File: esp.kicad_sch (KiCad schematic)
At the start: 13 parts, among them U3 ESP32-S3, U8 W25Q16JVUUIQ, Y1 40MHz 10pF

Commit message: finished Layout, started PCB design agound ESP32
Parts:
- added C24, C25: C, Capacitor_SMD:C_0402_1005Metric, symbol Device:C
- added L4: L, Inductor_SMD:L_0402_1005Metric, symbol Device:L
- added U9: RFANT3216120A5T, EasyEda:FILTER-SMD_1206-2P-L3.2-W1.6-L, symbol EasyEda:RFANT3216120A5T
- U8: footprint EasyEDA:USON-8_L4.0-W3.0-P0.80-BL_AT25SL321 -> EasyEda:USON-8_L4.0-W3.0-P0.80-BL_AT25SL321
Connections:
- net +3V3: now also U3.4 (CHIP_PU)
- net GND: now also C24.2, C25.2
- net at U3.1 (LNA_IN): now also C24.1, L4.1
- new net: C25.1, L4.2, U9.1
- no-connect marks 8 -> 9

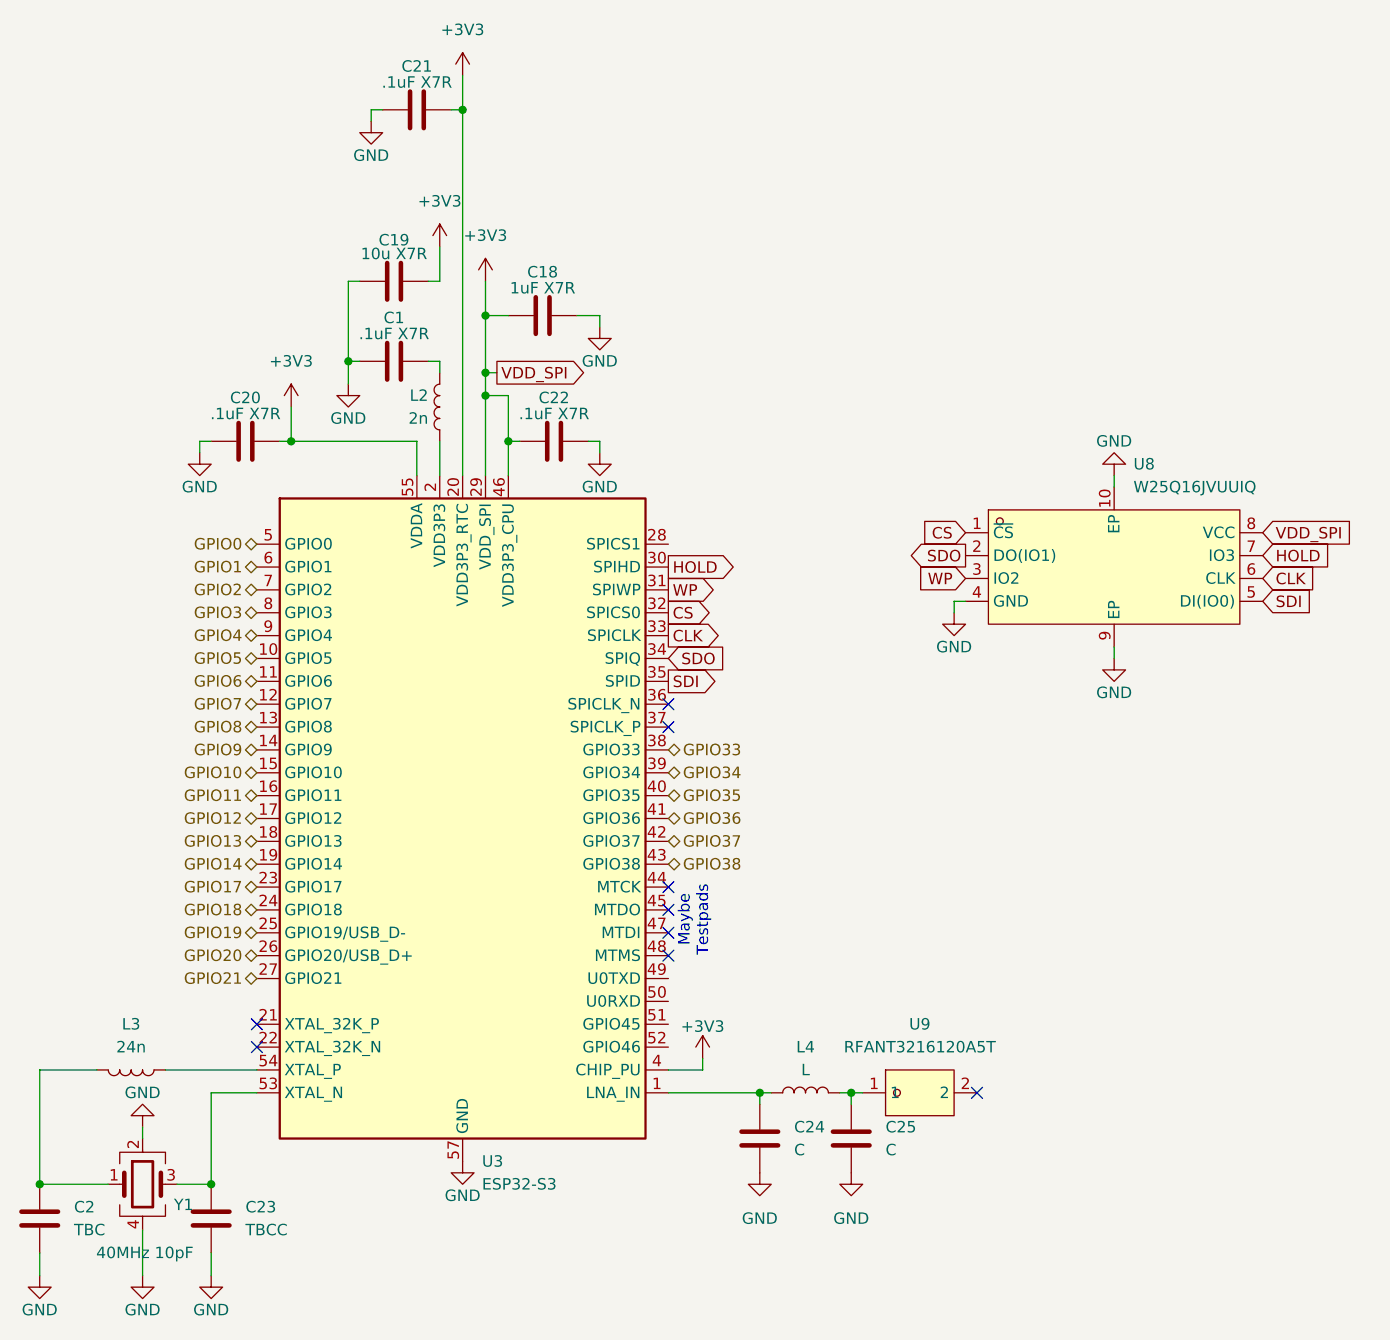
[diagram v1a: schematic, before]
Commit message: pcb parts placed not connected
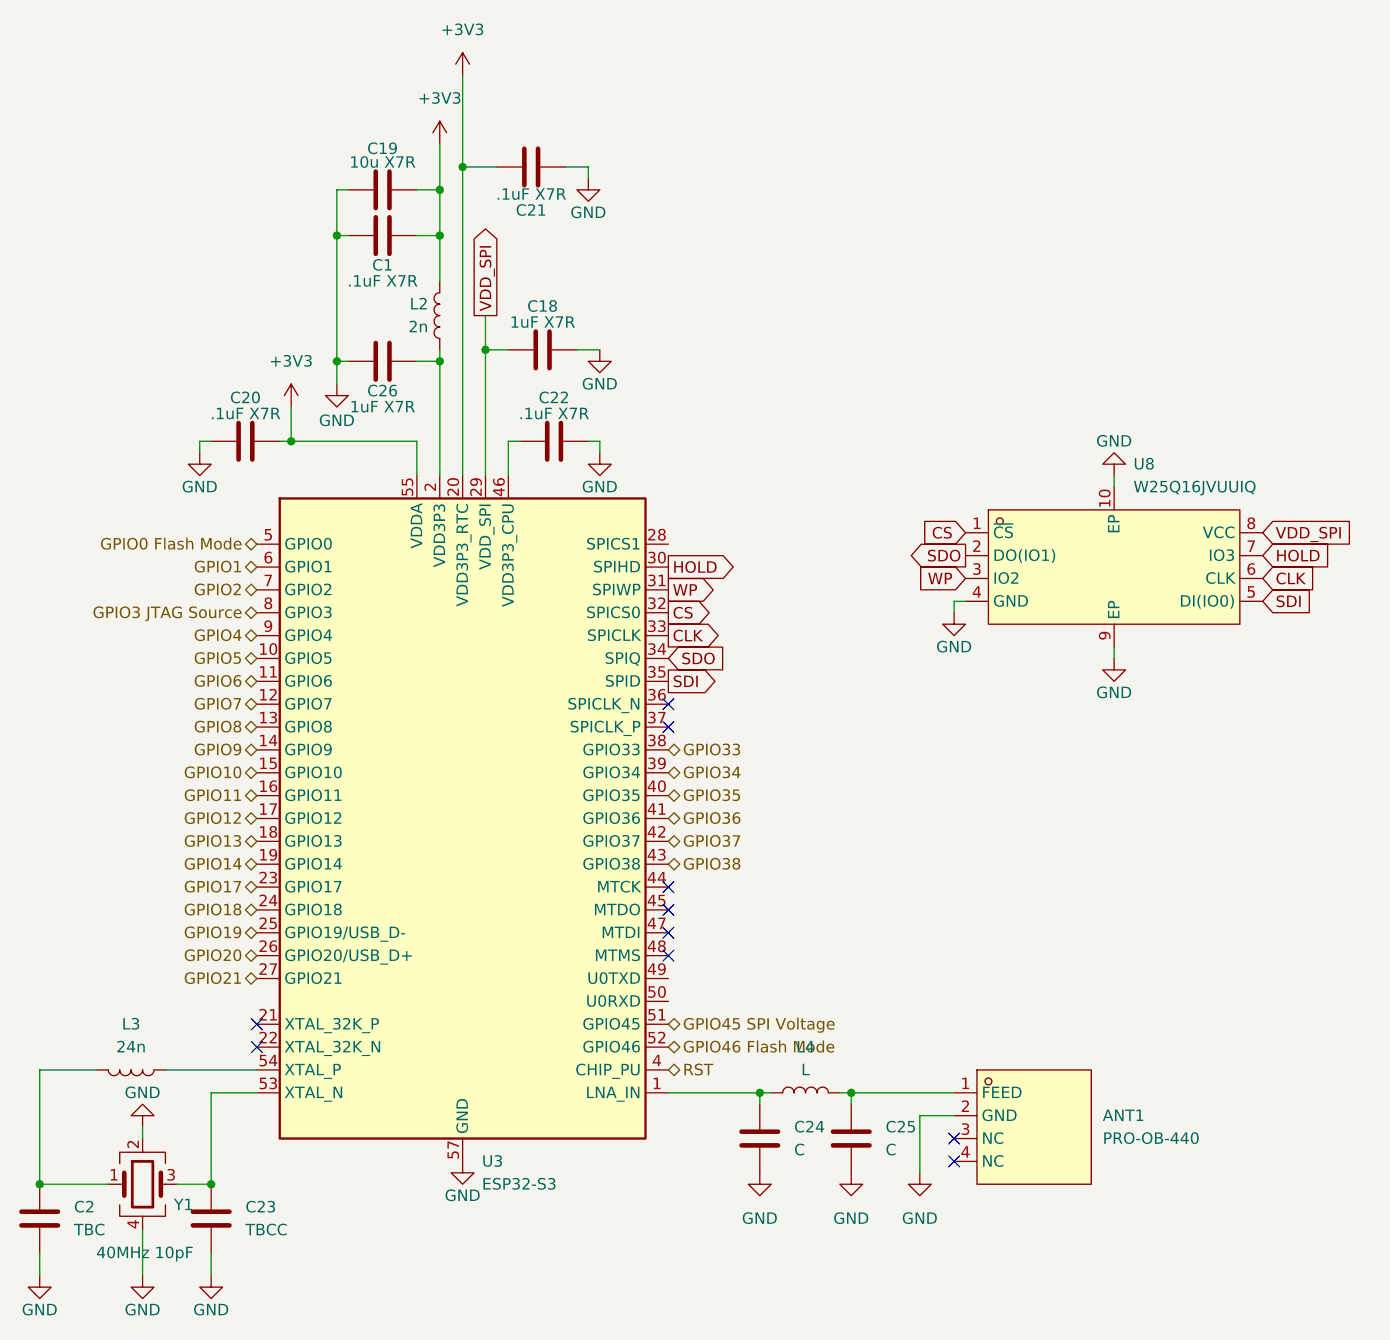
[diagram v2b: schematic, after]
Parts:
- removed U9: RFANT3216120A5T, EasyEda:FILTER-SMD_1206-2P-L3.2-W1.6-L, symbol EasyEda:RFANT3216120A5T
- added ANT1: PRO-OB-440, EasyEda:ANT-SMD_5P-L13.8-W5.2_PRO-OB-440, symbol EasyEda:PRO-OB-440
- added C26: 1uF X7R, Capacitor_SMD:C_0402_1005Metric, symbol Device:C
- U3: footprint Package_DFN_QFN:QFN-56-1EP_7x7mm_P0.4mm_EP4x4mm_ThermalVias -> Package_DFN_QFN:QFN-56-1EP_7x7mm_P0.4mm_EP4x4mm
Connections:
- net +3V3: now also C1.1, L2.1; no longer C18.1, C22.1, U3.29 (VDD_SPI), U3.4 (CHIP_PU), U3.46 (VDD3P3_CPU), U8.8 (VCC)
- net GND: now also ANT1.2 (GND), C26.1
- net at L2.2, U3.2 (VDD3P3), U3.3 (VDD3P3): now also C26.2
- net GPIO45 SPI Voltage: now reaches U3.51 (GPIO45)
- net GPIO46 Flash Mode: now reaches U3.52 (GPIO46)
- net at C25.1, L4.2: now also ANT1.1 (FEED)
- net GPIO0 renamed GPIO0 Flash Mode
- net GPIO3 renamed GPIO3 JTAG Source
- new net: C22.1, U3.46 (VDD3P3_CPU)
- new net RST: U3.4 (CHIP_PU)
- new net VDD_SPI: C18.1, U3.29 (VDD_SPI), U8.8 (VCC)
- no-connect marks 9 -> 10
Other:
- note removed: "Maybe Testpads"
- moved on the sheet: C1, C18, C19, C21, L2
